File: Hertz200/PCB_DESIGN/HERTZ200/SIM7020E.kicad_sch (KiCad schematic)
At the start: 29 parts

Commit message: Voltage_Shifter01
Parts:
- added C? (x2): 0.1uF, symbol Device:C_Small
- added D?: ESD9B5.0ST5G, Diode_SMD:D_SOD-923, symbol Diode:ESD9B5.0ST5G
- added U?: TXB0102DCU, Package_SO:VSSOP-8_2.3x2mm_P0.5mm, symbol Logic_LevelTranslator:TXB0102DCU
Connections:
- net +3V3: now also C?.1, U?.7 (VCCB)
- net GND: now also C?.2, C?.2, D?.1 (A1), U?.2 (GND)
- net at C?.1, J?.1, R?.2: now also D?.2 (A2)
- net UART1_TXD: now reaches U?.1 (UART1_TXD)
- net UART1_TXD: now also U?.5 (A1)
- net UART1_RDX: now reaches U?.2 (UART1_RXD)
- net UART1_RDX: now also U?.4 (A2)
- net VDD_EXT: now reaches U?.40 (VDD_EXT)
- net VDD_EXT: now also C?.1, U?.3 (VCCA), U?.6 (OE)
- new net SIM7020E_UART1_RXD: U?.1 (B2)
- new net SIM7020E_UART1_TXD: U?.8 (B1)
- no-connect marks 15 -> 14

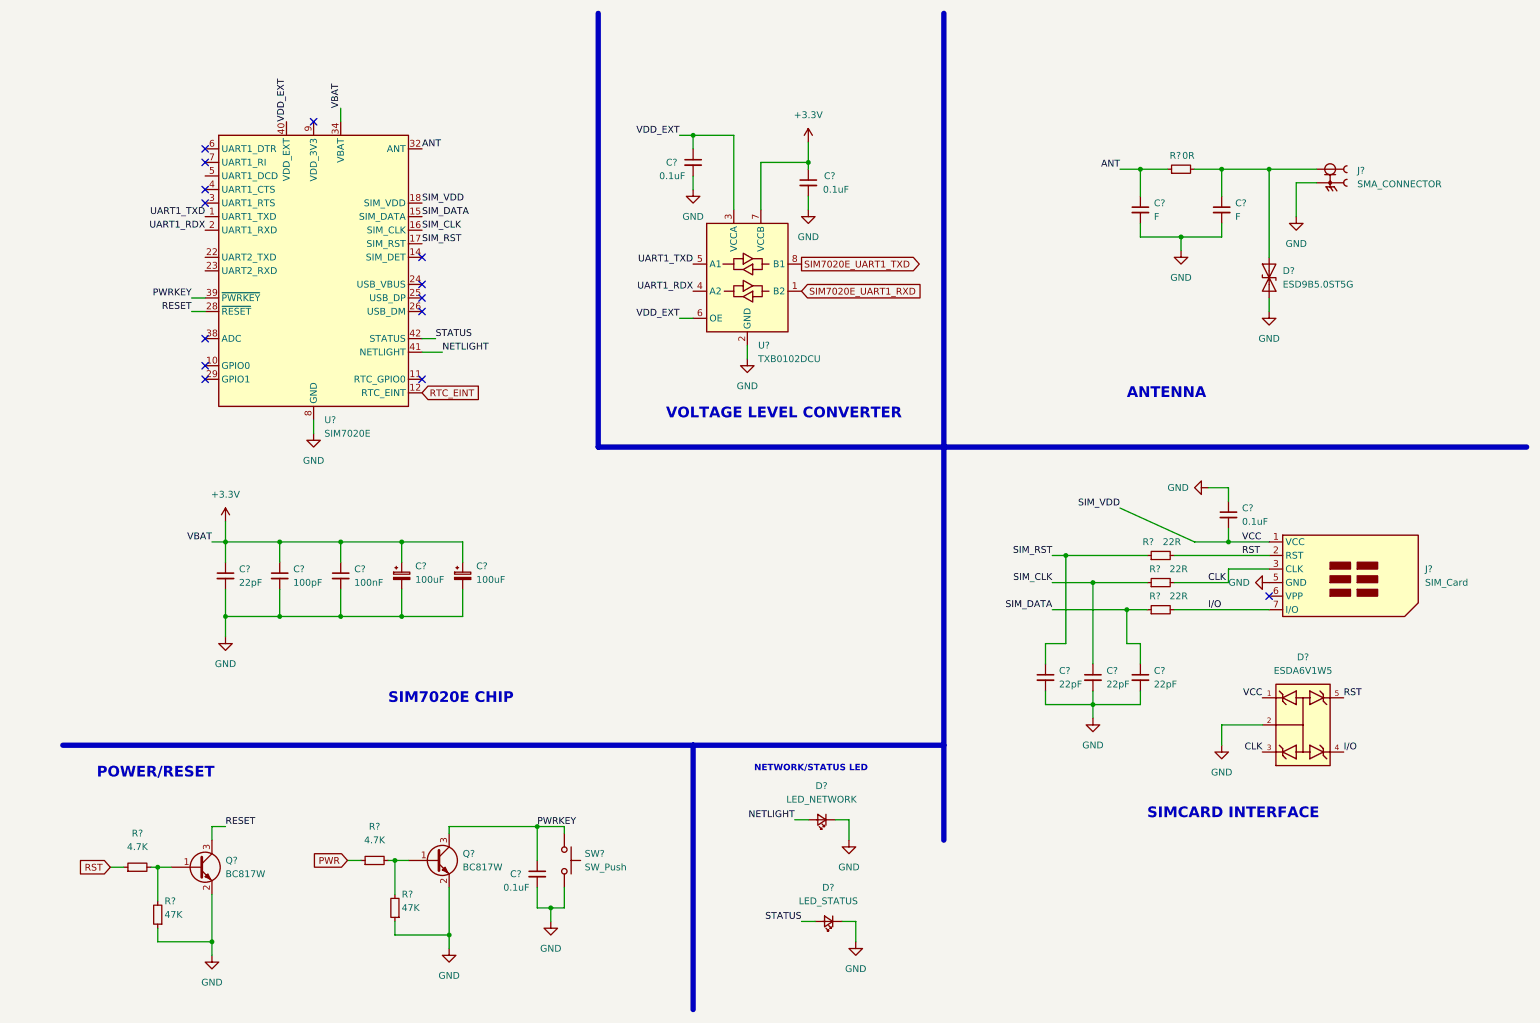
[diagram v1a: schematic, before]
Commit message: MCU-PIN-ASSIGNMENT
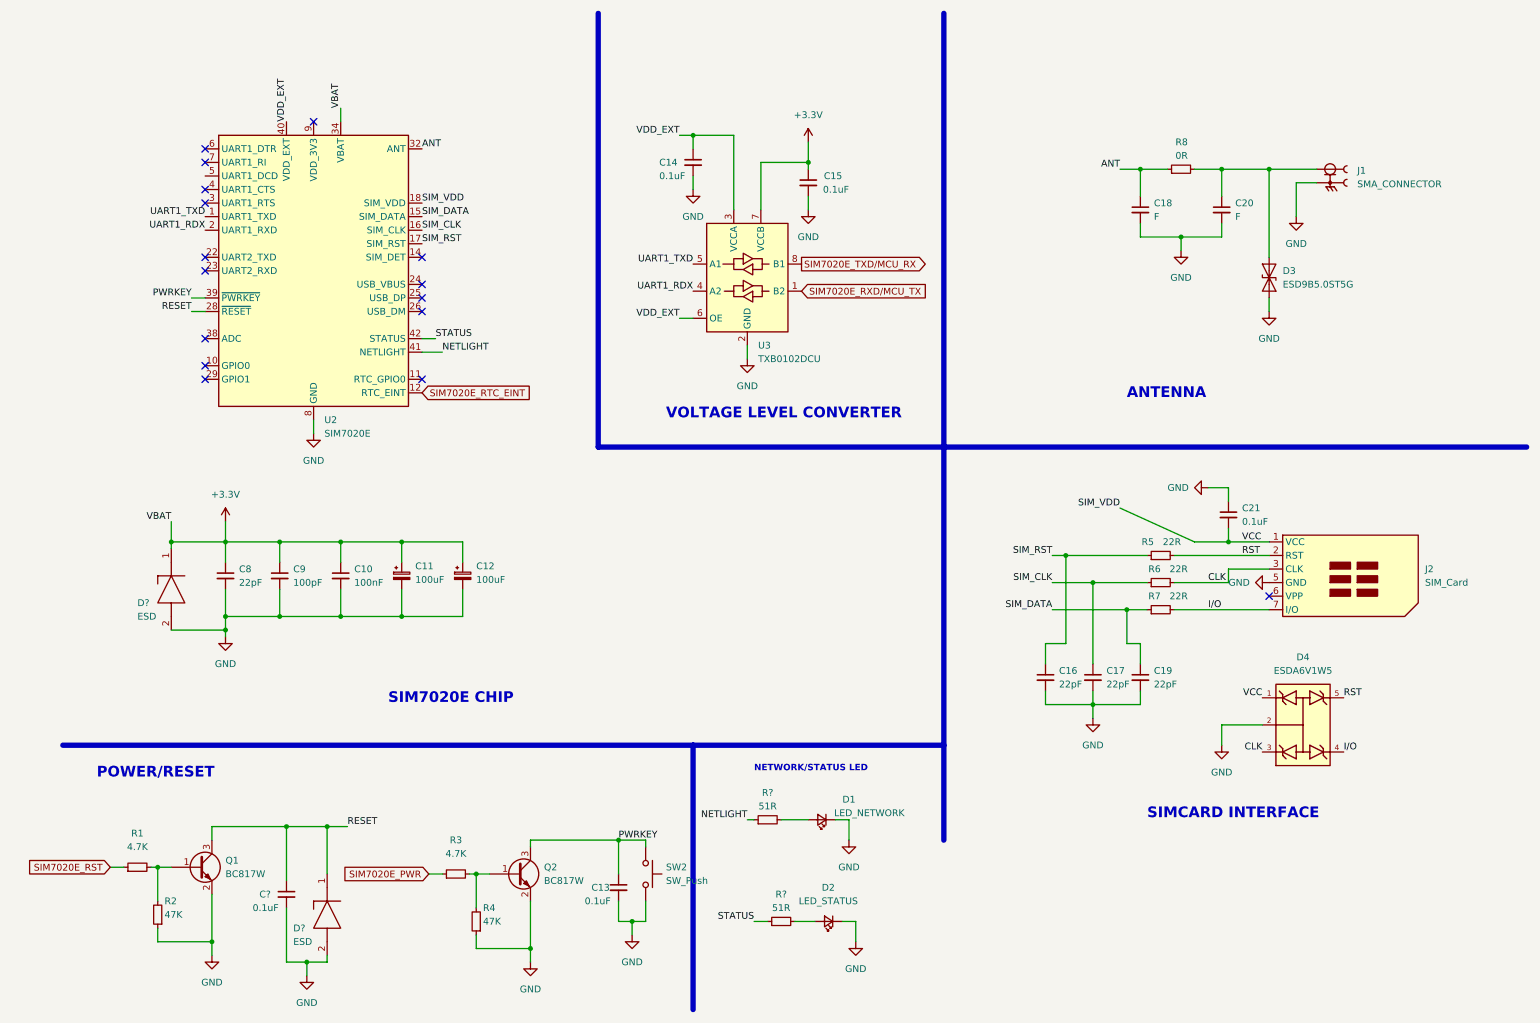
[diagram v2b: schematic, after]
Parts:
- added C?: 0.1uF, symbol Device:C_Small
- added D? (x2): ESD, SODFL1006X43N, symbol ESD:ESD3V3D9-TP
- added R? (x2): 51R, symbol Device:R_Small
- gave numbers to parts that had none: 33
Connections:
- net +3V3: now also D?.1
- net GND: now also C?.2, D?.2, D?.2
- net NETLIGHT: now also R?.1; no longer D1.2 (A)
- net RESET: now also C?.1, D?.1
- net RST: no longer R1.1
- net STATUS: now also R?.1; no longer D2.2 (A)
- net PWR renamed SIM7020E_PWR
- net RTC_EINT renamed SIM7020E_RTC_EINT
- net SIM7020E_UART1_RXD renamed SIM7020E_RXD/MCU_TX
- net SIM7020E_UART1_TXD renamed SIM7020E_TXD/MCU_RX
- new net: D1.2 (A), R?.2
- new net: D2.2 (A), R?.2
- new net SIM7020E_RST: R1.1
- no-connect marks 14 -> 16
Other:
- moved on the sheet: C13, Q2, R3, R4, SW2

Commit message: schamtics_finish
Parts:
- gave numbers to parts that had none: 5
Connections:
- net SIM7020E_UART2_TXD/u_RX: now reaches U2.22 (UART2_TXD)
- net SIM7020E_UART2_RXD/u_TX: now reaches U2.23 (UART2_RXD)
- net SIM7020E_GPIO1: now reaches U2.29 (GPIO1)
- no-connect marks 16 -> 14
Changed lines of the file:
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@@
   (junction (at 74.93 124.46) (diameter 0) (color 0 0 0 0)
   )
-  (no_connect (at 38.1 80.01))
   (no_connect (at 38.1 77.47))
   (no_connect (at 38.1 44.45))
@@
   (no_connect (at 237.49 120.65))
   (no_connect (at 78.74 80.01))
+  (no_connect (at 38.1 41.91))
   (no_connect (at 58.42 31.75))
   (no_connect (at 38.1 36.83))
@@
   (no_connect (at 78.74 57.15))
   (no_connect (at 38.1 72.39))
-  (no_connect (at 38.1 57.15))
-  (no_connect (at 38.1 59.69))
   (wire (pts (xy 229.87 107.95) (xy 229.87 110.49))
     (stroke (width 0) (type default) (color 0 0 0 0))
@@
     )
   )
+  (global_label "SIM7020E_UART2_RXD{slash}u_TX" (shape input) (at 38.1 59.69 180) (fields_autoplaced)
+    (effects (font (size 1.27 1.27)) (justify right))
+    (property "Intersheet References" "${INTERSHEET_REFS}" (id 0) (at 9.2588 59.6106 0)
+      (effects (font (size 1.27 1.27)) (justify right) hide)
+    )
+  )
   (global_label "SIM7020E_TXD{slash}MCU_RX" (shape output) (at 149.86 58.42 0) (fields_autoplaced)
     (effects (font (size 1.27 1.27)) (justify left))
@@
     )
   )
+  (global_label "SIM7020E_UART2_TXD{slash}u_RX" (shape output) (at 38.1 57.15 180) (fields_autoplaced)
+    (effects (font (size 1.27 1.27)) (justify right))
+    (property "Intersheet References" "${INTERSHEET_REFS}" (id 0) (at 9.2588 57.0706 0)
+      (effects (font (size 1.27 1.27)) (justify right) hide)
+    )
+  )
   (global_label "SIM7020E_RXD{slash}MCU_TX" (shape input) (at 149.86 63.5 0) (fields_autoplaced)
     (effects (font (size 1.27 1.27)) (justify left))
@@
     )
   )
+  (global_label "SIM7020E_GPIO1" (shape bidirectional) (at 38.1 80.01 180) (fields_autoplaced)
+    (effects (font (size 1.27 1.27)) (justify right))
+    (property "Intersheet References" "${INTERSHEET_REFS}" (id 0) (at 19.7817 79.9306 0)
+      (effects (font (size 1.27 1.27)) (justify right) hide)
+    )
+  )
   (symbol (lib_id "power:GND") (at 158.75 166.37 0) (unit 1)
     (in_bom yes) (on_board yes) (fields_autoplaced)
@@
   (symbol (lib_id "ESD:ESD3V3D9-TP") (at 60.96 172.72 270) (unit 1)
     (in_bom yes) (on_board yes)
-    (property "Reference" "D?" (id 0) (at 54.61 182.88 90)
+    (property "Reference" "D9" (id 0) (at 54.61 182.88 90)
       (effects (font (size 1.27 1.27)) (justify left))
     )
@@
   (symbol (lib_id "ESD:ESD3V3D9-TP") (at 31.75 111.76 270) (unit 1)
     (in_bom yes) (on_board yes)
-    (property "Reference" "D?" (id 0) (at 25.4 121.92 90)
+    (property "Reference" "D6" (id 0) (at 25.4 121.92 90)
       (effects (font (size 1.27 1.27)) (justify left))
     )
@@
   (symbol (lib_id "power:GND") (at 57.15 191.77 0) (unit 1)
     (in_bom yes) (on_board yes) (fields_autoplaced)
-    (property "Reference" "#PWR?" (id 0) (at 57.15 198.12 0)
+    (property "Reference" "#PWR056" (id 0) (at 57.15 198.12 0)
       (effects (font (size 1.27 1.27)) hide)
     )
@@
   (symbol (lib_id "Device:R_Small") (at 143.51 162.56 90) (unit 1)
     (in_bom yes) (on_board yes)
-    (property "Reference" "R?" (id 0) (at 143.51 157.48 90))
+    (property "Reference" "R26" (id 0) (at 143.51 157.48 90))
     (property "Value" "51R" (id 1) (at 143.51 160.02 90))
     (property "Footprint" "" (id 2) (at 143.51 162.56 0)
@@
   (symbol (lib_id "Device:R_Small") (at 146.05 181.61 90) (unit 1)
     (in_bom yes) (on_board yes)
-    (property "Reference" "R?" (id 0) (at 146.05 176.53 90))
+    (property "Reference" "R27" (id 0) (at 146.05 176.53 90))
     (property "Value" "51R" (id 1) (at 146.05 179.07 90))
     (property "Footprint" "" (id 2) (at 146.05 181.61 0)
@@
   (symbol (lib_id "Device:C_Small") (at 53.34 176.53 0) (unit 1)
     (in_bom yes) (on_board yes)
-    (property "Reference" "C?" (id 0) (at 48.26 176.53 0)
-      (effects (font (size 1.27 1.27)) (justify left))
-    )
+    (property "Reference" "C39" (id 0) (at 48.26 176.53 0)
+      (effects (font (size 1.27 1.27)) (justify left))
+    )

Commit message: Component_selection
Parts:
- removed C39: 0.1uF, symbol Device:C_Small
- removed D3: ESD9B5.0ST5G, Diode_SMD:D_SOD-923, symbol Diode:ESD9B5.0ST5G
- removed D9: ESD, SODFL1006X43N, symbol ESD:ESD3V3D9-TP
- removed Q1: BC817W, Package_TO_SOT_SMD:SOT-323_SC-70, symbol Transistor_BJT:BC817W
- removed R1: 4.7K, symbol Device:R_Small
- removed R2: 47K, symbol Device:R_Small
- added D3: ESD, symbol ESD:ESD3V3D9-TP
- C10, C13, C14, C15, C16, C17, C18, C19, C20, C21: footprint (none) -> Capacitor_SMD:C_0603_1608Metric
- C8, C9: footprint (none) -> Capacitor_SMD:C_0402_1005Metric
- D1, D2: footprint (none) -> LED_SMD:LED_0805_2012Metric
- D4: footprint SOT65P210X110-5N -> (none)
- D6: footprint SODFL1006X43N -> (none)
- J1: footprint LPRS_SMA_CONNECTOR -> (none)
- R26, R27: value 51R -> 33R; footprint (none) -> Resistor_SMD:R_0603_1608Metric
- R3, R4, R5, R6, R7, R8: footprint (none) -> Resistor_SMD:R_0603_1608Metric
- SW2: footprint (none) -> TS04-66-75-BK-160-SMT:SW_TS04-66-75-BK-160-SMT
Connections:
- net GND: now also D3.2
- net at C20.1, J1.1, R8.2: now also D3.1
- net RESET: no longer names the net of U2.28 (~{RESET})
- no-connect marks 14 -> 15
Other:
- moved on the sheet: C13, Q2, R3, R4, SW2, U2

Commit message: layout
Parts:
- removed Q2: BC817W, Package_TO_SOT_SMD:SOT-323_SC-70, symbol Transistor_BJT:BC817W
- removed U3: TXB0102DCU, Package_SO:VSSOP-8_2.3x2mm_P0.5mm, symbol Logic_LevelTranslator:TXB0102DCU
- added Q2: BC847, Package_TO_SOT_SMD:SOT-23, symbol Transistor_BJT:BC847
- added U3: TXB0104PW, Package_SO:TSSOP-14_4.4x5mm_P0.65mm, symbol Logic_LevelTranslator:TXB0104PW
- C11, C12: footprint (none) -> T491X107K025AT:CAPMP7343X400N
- D3, D6: footprint (none) -> Diode_SMD:D_0603_1608Metric
- D4: footprint (none) -> ESDA6V1W5:SOT65P210X110-5N
- J1: footprint (none) -> SMA_CONNECTOR:LPRS_SMA_CONNECTOR
- J2: footprint (none) -> 503960-0696:5039600696
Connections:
- net +3V3: now also U3.14 (VCCB)
- net GND: now also Q2.2 (E), U3.7 (GND)
- net PWRKEY: now also Q2.3 (C)
- net SIM7020E_RXD/MCU_TX: now also U3.12 (B2)
- net SIM7020E_TXD/MCU_RX: now also U3.13 (B1)
- net SIM7020E_UART2_RXD/u_TX: now also U3.10 (B4); no longer U2.23 (UART2_RXD)
- net SIM7020E_UART2_TXD/u_RX: now also U3.11 (B3); no longer U2.22 (UART2_TXD)
- net UART1_RDX: now also U3.3 (A2)
- net UART1_TXD: now also U3.2 (A1)
- net VDD_EXT: now also U3.1 (VCCA), U3.8 (OE)
- net at R3.2, R4.2: now also Q2.1 (B)
- net CLK renamed CLK_SC
- net I/O renamed I/O_SC
- net RST renamed RST_SC
- net SIM_VDD renamed SC_VCC
- new net UART2_RDX: U2.23 (UART2_RXD), U3.5 (A4)
- new net UART2_TXD: U2.22 (UART2_TXD), U3.4 (A3)
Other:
- moved on the sheet: C14, C15
